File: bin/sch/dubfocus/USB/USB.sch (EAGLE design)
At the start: 3 parts

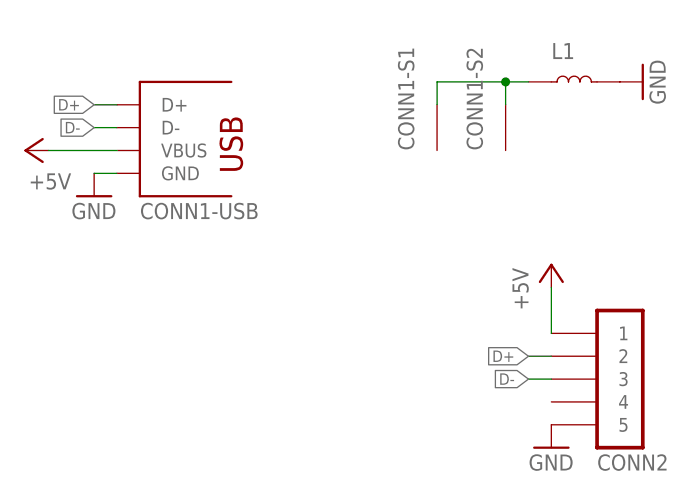
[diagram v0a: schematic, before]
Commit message: targets: update schematics for dubfocus
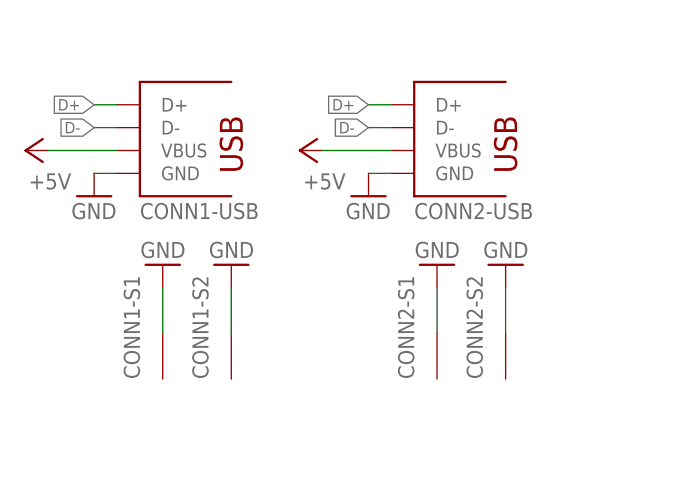
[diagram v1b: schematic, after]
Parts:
- removed L1: FERRITE_BEAD-BLM21PG221SN1D, igor_lbr:FERRITE_BEAD-BLM21PG221SN1D
- CONN1: value USB-V -> USB-B-V; device igor_lbr:USB-V -> igor_lbr:USB-B-V
- CONN2: value PINHD-1X05-JST-XH-H -> USB-A-H; device igor_lbr:PINHD-1X05-JST-XH-H -> igor_lbr:USB-A-H
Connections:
- removed net N$1: CONN1-S1.S, CONN1-S2.S, L1.1
- net +5V: now also CONN2-USB.VBUS; no longer CONN2.1
- net D+: now also CONN2-USB.D+; no longer CONN2.2
- net D-: now also CONN2-USB.D-; no longer CONN2.3
- net GND: now also CONN1-S1.S, CONN1-S2.S, CONN2-S1.S, CONN2-S2.S, CONN2-USB.GND; no longer CONN2.5, L1.2
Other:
- moved on the sheet: CONN1-S1, CONN1-S2
